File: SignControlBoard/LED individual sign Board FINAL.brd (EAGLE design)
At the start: 35.4 x 31.7 mm, 25 parts, among them U1 ATMEGA328P, U2 M5205 5v, X1 22-23-2021, Y1 16MHz

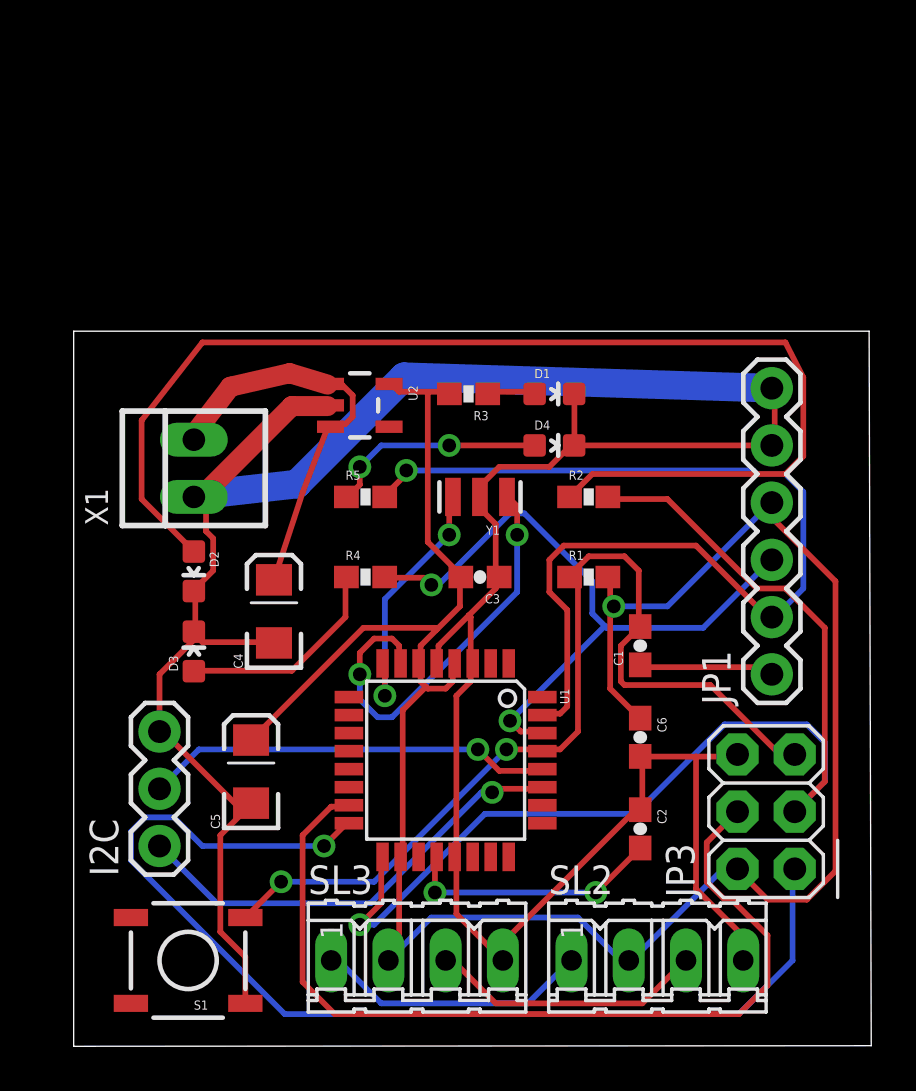
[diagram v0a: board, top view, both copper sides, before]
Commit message: Updated control and sign boards. Removed old versions
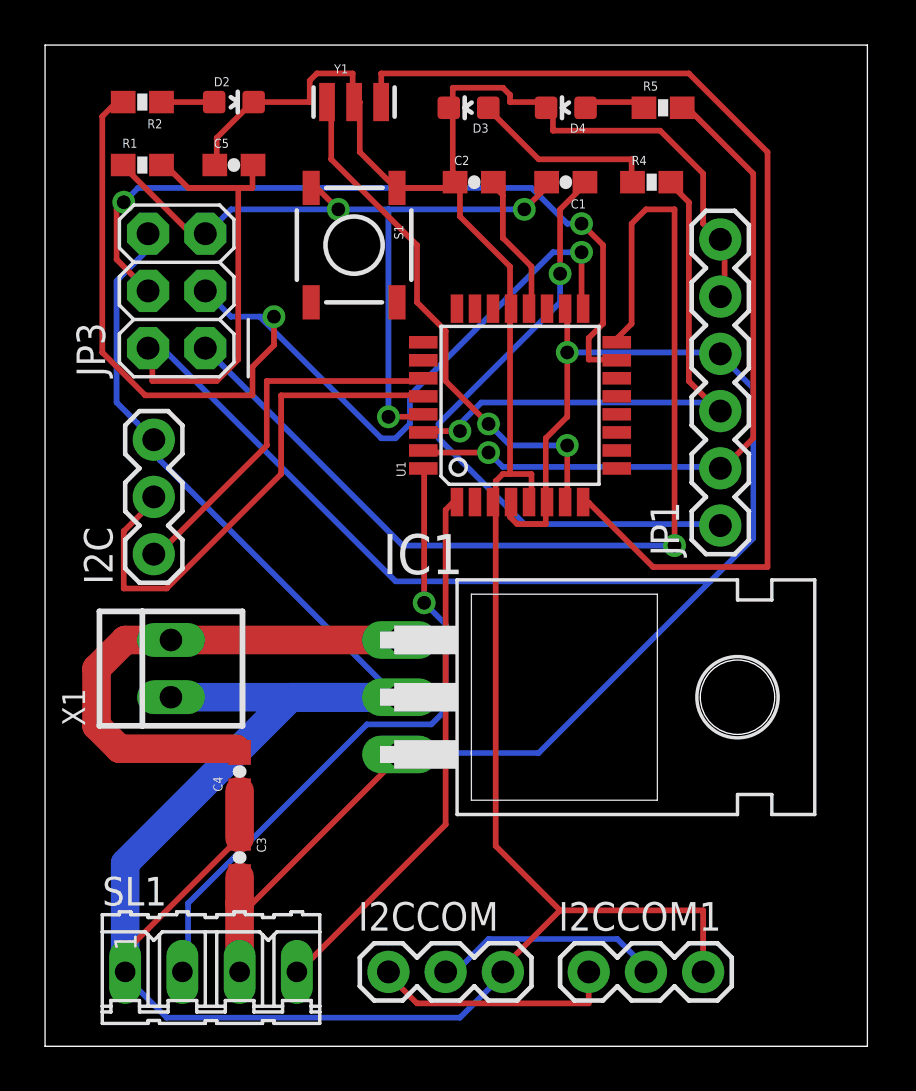
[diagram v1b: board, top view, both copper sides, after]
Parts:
- removed C6: 0.1uF, SparkFun-Passives:0603-CAP
- removed D1: Power, SparkFun-LED:LED-0603
- removed R3: 10k, SparkFun-Passives:0603-RES
- removed SL2, SL3: (no value), con-amp-quick:04P
- removed U2: M5205 5v, SparkFun-PowerIC:SOT23-5
- added I2CCOM, I2CCOM1: (no value), SparkFun-Connectors:1X03
- added IC1: 7805T, linear:TO220H
- added SL1: (no value), con-amp-quick:04P
- C4: value 10uF -> 0.33uF; device SparkFun-Passives:EIA3216 -> SparkFun-Passives:0603-CAP
- C5: value 10uF -> 0.1uF; device SparkFun-Passives:EIA3216 -> SparkFun-Passives:0603-CAP
- moved JP3 34.9 mm to (4.57, 33.5)
- moved S1 32.6 mm to (12.4, 35.6), turned to 270 degrees
- moved C2 29.6 mm to (17.8, 38.4), turned to 0 degrees
- moved D3 27.0 mm to (17.5, 41.7), turned to 90 degrees
- moved R1 27.0 mm to (3.05, 39.1)
- moved C5 26.9 mm to (7.11, 39.1), turned to 0 degrees
- moved R2 26.5 mm to (3.05, 41.9), turned to 180 degrees
- moved R5 21.7 mm to (26.2, 41.7)
- moved R4 21.6 mm to (25.7, 38.4)
- moved D2 20.9 mm to (7.11, 41.9), turned to 270 degrees
- moved C1 20.8 mm to (21.8, 38.4), turned to 180 degrees
- moved Y1 18.4 mm to (12.4, 41.9), turned to 0 degrees
- moved C3 16.4 mm to (7.37, 8.38), turned to 270 degrees
- moved U1 16.1 mm to (19.8, 28.4), turned to 90 degrees
- moved D4 15.0 mm to (21.8, 41.7), turned to 90 degrees
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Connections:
- removed net N$3: D1.A, R3.1
- net D2: now also SL1.2
- net D3: now also SL1.4
- net GND: now also C4.1, C5.1, I2CCOM.3, I2CCOM1.3, IC1.2, SL1.1; no longer C4.C, C5.C, C6.2, D1.C, SL2.4, SL3.4, U2.2
- net SCA: now also I2CCOM.1, I2CCOM1.1; no longer SL2.1, SL3.1
- net SDL: now also I2CCOM.2, I2CCOM1.2; no longer SL2.3, SL3.3
- net VCC: now also C5.2, IC1.3, SL1.3; no longer C5.A, C6.1, R3.2, SL2.2, SL3.2, U2.5
- net VIN: now also C4.2, IC1.1; no longer C4.A, U2.1, U2.3
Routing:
- net N$4: track 53.4 -> 2.34 mm
- net GND: track 138.3 -> 177.4 mm
- net N$2: track 11.6 -> 47.7 mm, vias 2 -> 0
- net D2: track 0.00 -> 29.3 mm, vias 0 -> 1
- net D3: track 0.00 -> 23.9 mm
- net DTR: track 6.02 -> 28.1 mm, vias 0 -> 1
- net TXO: track 45.3 -> 31.6 mm
- net RESET: track 44.0 -> 33.5 mm, vias 2 -> 3
- net VCC: track 100.8 -> 109.9 mm
- net N$6: track 9.76 -> 2.85 mm, vias 2 -> 0
- net MOSI: track 40.4 -> 33.8 mm, vias 0 -> 2
- net RXI: track 30.5 -> 25.1 mm, vias 2 -> 1
- net SCL: track 18.2 -> 23.5 mm, vias 1 -> 0
- net VIN: track 18.1 -> 23.4 mm
- net AREF: track 11.5 -> 6.31 mm, vias 2 -> 0
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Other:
- board size 35.4 x 31.7 mm -> 36.5 x 44.4 mm
